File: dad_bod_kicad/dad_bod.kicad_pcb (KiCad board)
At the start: 2 copper layers, 89.2 x 89 mm, 132 parts, among them J1 Conn_01x01, J10 Conn_01x03_Male, J11 BNC5-J-P-GN-RA-BH2D, J12 USB4085-GF-A_REVA4, J13 Conn_01x03_Male, J14 Conn_01x03_Male, J2 Conn_01x01, J3 Conn_01x01, J4 Conn_01x01, J5 Conn_01x03_Male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

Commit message: fixing scheme & pcb disparities
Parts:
- C1: footprint ECQ-UBAF4747K_kicad:ECQ-UBAF474K-3_side -> kyuditsky_kicad:ECQ-UBAF474K-3_side
- D2, D3, D4, D5: footprint Diode_THT:D_DO-41_SOD81_P2.54mm_Vertical_AnodeUp -> Diode_THT:D_DO-41_SOD81_P2.54mm_Vertical_KathodeUp
- FB1, FB2, FB3: footprint Resistor_SMD:R_0603_1608Metric_Pad1.05x0.95mm_HandSolder -> Resistor_SMD:R_0805_2012Metric_Pad1.20x1.40mm_HandSolder
- J12: footprint kyuditsky_kicad_fp:GCT_USB4085-GF-A_REVA4 -> kyuditsky_kicad:GCT_USB4085-GF-A_REVA4
- U1: footprint kyuditsky_kicad_fp:SL1002A600SP -> kyuditsky_kicad:SL1002A600SP
- moved C3 13.1 mm to (130.3, 133.3)
- moved R1 13.1 mm to (122.7, 133.3)
- moved C18 13.1 mm to (122.0, 124.1)
- moved F1 13.1 mm to (145.4, 134.1)
- moved J3 13.1 mm to (94.5, 131.7)
- moved J4 13.1 mm to (109.2, 131.7)
- moved R13 13.1 mm to (126.7, 124.1)
- moved R40 13.1 mm to (137.7, 136.7)
- moved C17 13.1 mm to (141.5, 117.3)
- moved C34 13.1 mm to (138.4, 96.8)
- moved C42 13.1 mm to (141.0, 71.8)
- moved R10 13.1 mm to (133.6, 112.6)
- moved R12 13.1 mm to (133.6, 117.3)
- moved R28 13.1 mm to (133.6, 96.8)
- moved C10 13.1 mm to (122.2, 111.1)
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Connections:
- C18 pad 1: Net-(C18-Pad1) -> DIVin2-
- J12 pad A8: Net-(J12-PadA8) -> unconnected-(J12-PadA8)
- J12 pad B8: Net-(J12-PadB8) -> unconnected-(J12-PadB8)
- J13 pad 3: Net-(J13-Pad3) -> unconnected-(J13-Pad3)
- J14 pad 3: Net-(J14-Pad3) -> unconnected-(J14-Pad3)
- R13 pad 2: Net-(C18-Pad1) -> DIVin2-
- T1 pad 2: Net-(T1-Pad2) -> unconnected-(T1-Pad2)
- T1 pad 5: Net-(T1-Pad5) -> unconnected-(T1-Pad5)

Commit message: new layout
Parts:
- J9: footprint Connector_PinSocket_2.54mm:PinSocket_2x15_P2.54mm_Horizontal -> Connector_PinSocket_2.54mm:PinSocket_2x15_P2.54mm_Vertical
- moved RV1 80.3 mm to (78.5, 69.3), turned to 180 degrees
- moved U1 75.9 mm to (88.9, 68.6)
- moved T1 74.5 mm to (94.0, 79.0), turned to 90 degrees
- moved J11 71.5 mm to (97.8, 126.5), turned to 180 degrees
- moved D1 69.8 mm to (99.1, 68.3), turned to 0 degrees
- moved C2 69.6 mm to (98.3, 63.8), turned to 180 degrees
- moved C50 68.6 mm to (99.3, 115.8)
- moved C51 68.6 mm to (96.5, 115.8)
- moved C53 68.6 mm to (91.4, 115.8)
- moved Q3 68.6 mm to (102.4, 115.8)
- moved C52 68.6 mm to (94.0, 115.8)
- moved C49 68.6 mm to (88.9, 115.8)
- moved FB1 68.6 mm to (98.0, 119.0)
- moved FB3 68.6 mm to (98.1, 112.8)
- moved D6 65.8 mm to (73.9, 121.9), turned to -90 degrees
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
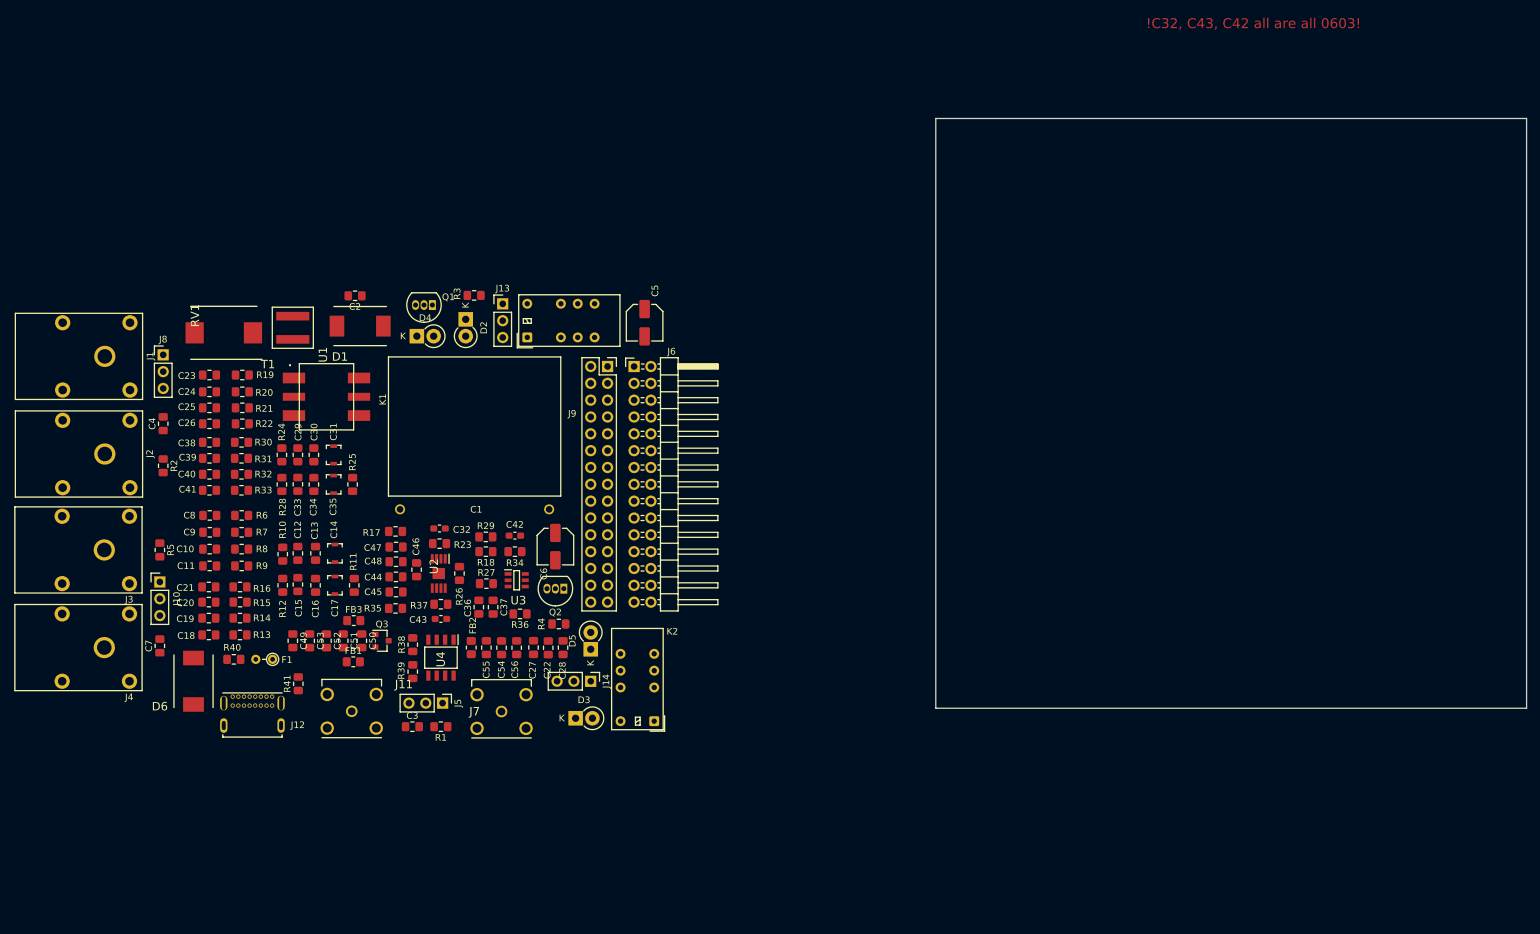
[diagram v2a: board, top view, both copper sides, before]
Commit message: Routed board
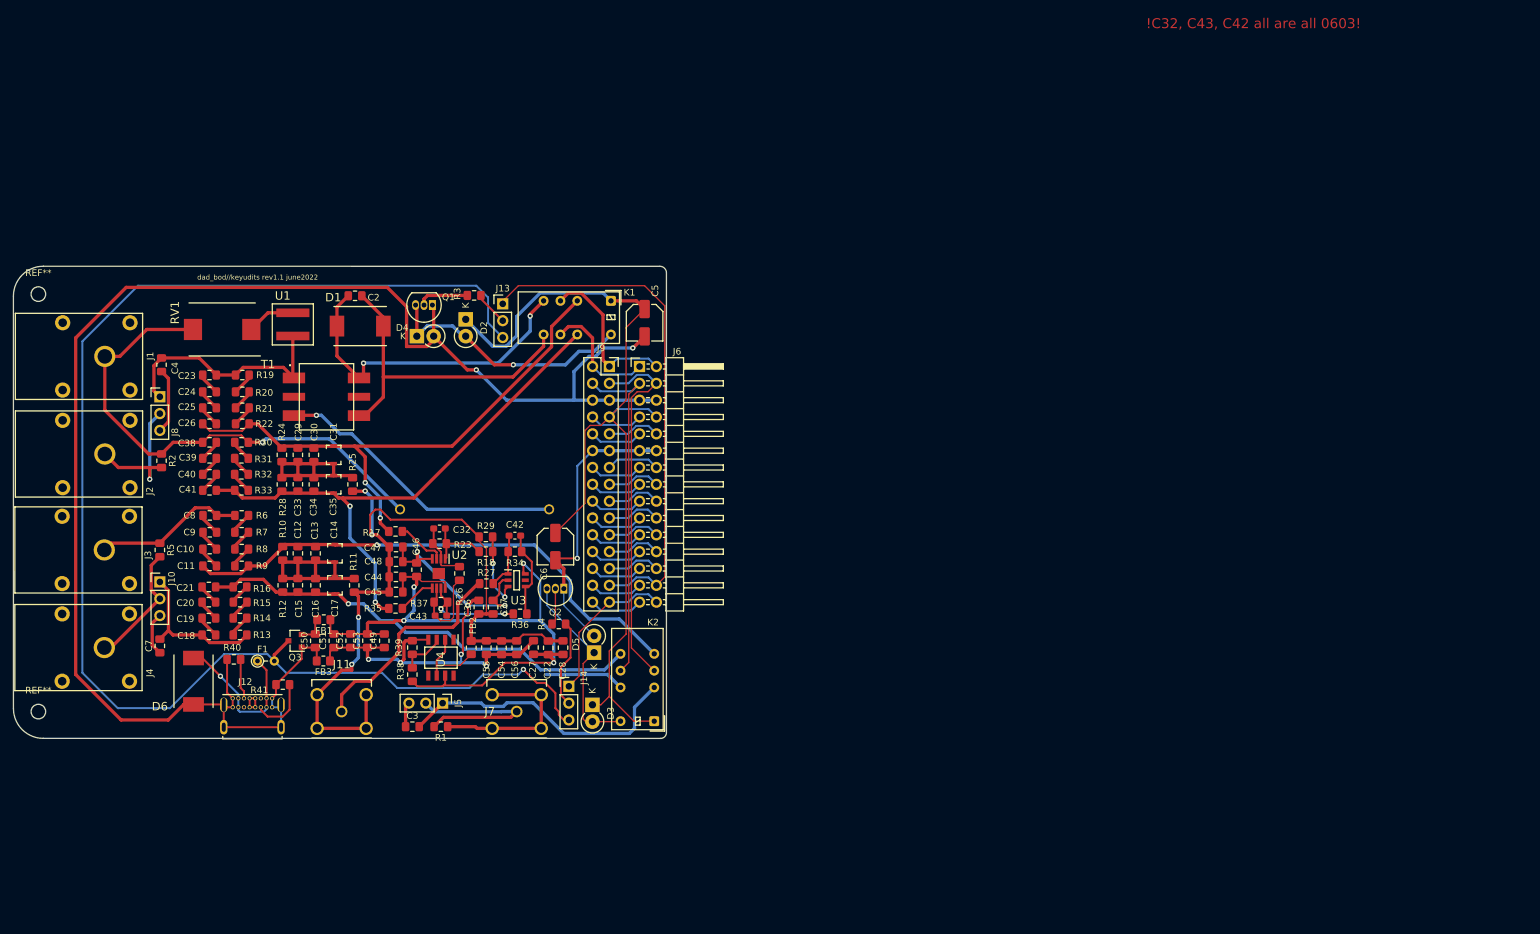
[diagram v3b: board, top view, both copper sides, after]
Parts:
- added REF**: MountingHole_2.2mm_M2, MountingHole:MountingHole_2.2mm_M2, F.Cu at (50.5, 63.5)
- added REF**: MountingHole_2.2mm_M2, MountingHole:MountingHole_2.2mm_M2, F.Cu at (50.5, 126.5)
- C1: moved to B.Cu
- moved C49 13.8 mm to (102.7, 115.8), turned to 90 degrees
- moved K1 13.8 mm to (136.9, 64.5), turned to -90 degrees
- moved Q3 13.1 mm to (89.2, 115.8), turned to 180 degrees
- moved C4 8.90 mm to (69.1, 74.2)
- moved C53 8.72 mm to (100.2, 115.8), turned to 90 degrees
- moved FB1 7.76 mm to (93.6, 112.6), turned to 180 degrees
- moved FB3 7.63 mm to (93.5, 118.9), turned to 180 degrees
- moved C50 7.03 mm to (92.3, 115.8), turned to 90 degrees
- moved J8 6.36 mm to (68.8, 79.0)
- moved R38 4.52 mm to (106.9, 120.9), turned to -90 degrees
- moved C52 3.64 mm to (97.6, 115.8), turned to 90 degrees
- moved R39 3.64 mm to (106.9, 116.8), turned to 90 degrees
- moved J14 3.39 mm to (130.6, 122.7), turned to 0 degrees
- moved D3 3.25 mm to (134.1, 125.5), turned to -90 degrees
- moved R41 2.34 mm to (87.4, 122.4), turned to 180 degrees
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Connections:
- J13 pad 2: V+ -> Net-(J13-Pad2)
- J13 pad 3: unconnected-(J13-Pad3) -> V+
- J14 pad 2: V+ -> Net-(R4-Pad1)
- J14 pad 3: unconnected-(J14-Pad3) -> V+
- J9 pad 1: scope1- -> scope1+
- J9 pad 10: waveform1 -> waveform2
- J9 pad 13: trigger2 -> trigger1
- J9 pad 14: trigger1 -> trigger2
- J9 pad 15: 8 -> 0
- J9 pad 16: 0 -> 8
- J9 pad 17: 9 -> 1
- J9 pad 18: 1 -> 9
- J9 pad 19: 10 -> 2
- J9 pad 2: scope1+ -> scope1-
- J9 pad 20: 2 -> 10
- J9 pad 21: 11 -> 3
- J9 pad 22: 3 -> 11
- J9 pad 23: 12 -> 4
- J9 pad 24: 4 -> 12
- J9 pad 25: 13 -> 5
- J9 pad 26: 5 -> 13
- J9 pad 27: 14 -> CV6
- J9 pad 28: CV6 -> 14
- J9 pad 29: 15 -> CV7
- J9 pad 3: scope2- -> scope2+
- J9 pad 30: CV7 -> 15
- J9 pad 4: scope2+ -> scope2-
- J9 pad 7: dad_V- -> relaypwr
- J9 pad 8: relaypwr -> dad_V-
- J9 pad 9: waveform2 -> waveform1
- R11 pad 1: GND -> GNDREF
- R3 pad 1: CV6 -> Net-(J13-Pad2)
- R4 pad 1: CV7 -> Net-(R4-Pad1)
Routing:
- net GND: track 0.00 -> 297.1 mm, vias 0 -> 3
- net V+: track 0.00 -> 213.4 mm, vias 0 -> 1
- net relaypwr: track 0.00 -> 138.8 mm
- net GNDREF: track 0.00 -> 116.2 mm, vias 0 -> 4
- net VCC: track 0.00 -> 104.6 mm, vias 0 -> 4
- net greg: track 0.00 -> 90.1 mm, vias 0 -> 7
- net DIVout1-: track 0.00 -> 86.2 mm, vias 0 -> 2
- net DIVout1+: track 0.00 -> 84.9 mm, vias 0 -> 2
- net DIVout2+: track 0.00 -> 79.0 mm, vias 0 -> 1
- net CV6: track 0.00 -> 77.9 mm
- net DIVin1-: track 0.00 -> 76.6 mm, vias 0 -> 1
- net DIVout2-: track 0.00 -> 68.2 mm, vias 0 -> 1
- net scope2+: track 0.00 -> 55.4 mm
- net scope2-: track 0.00 -> 52.6 mm
- net PLCout+: track 0.00 -> 49.6 mm, vias 0 -> 2
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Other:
- board size 89.2 x 89 mm -> 98.5 x 71.3 mm
- board text added: "JLCJLCJLCJLC"
- board text added: "dad_bod//keyudits rev1.1 june2022"

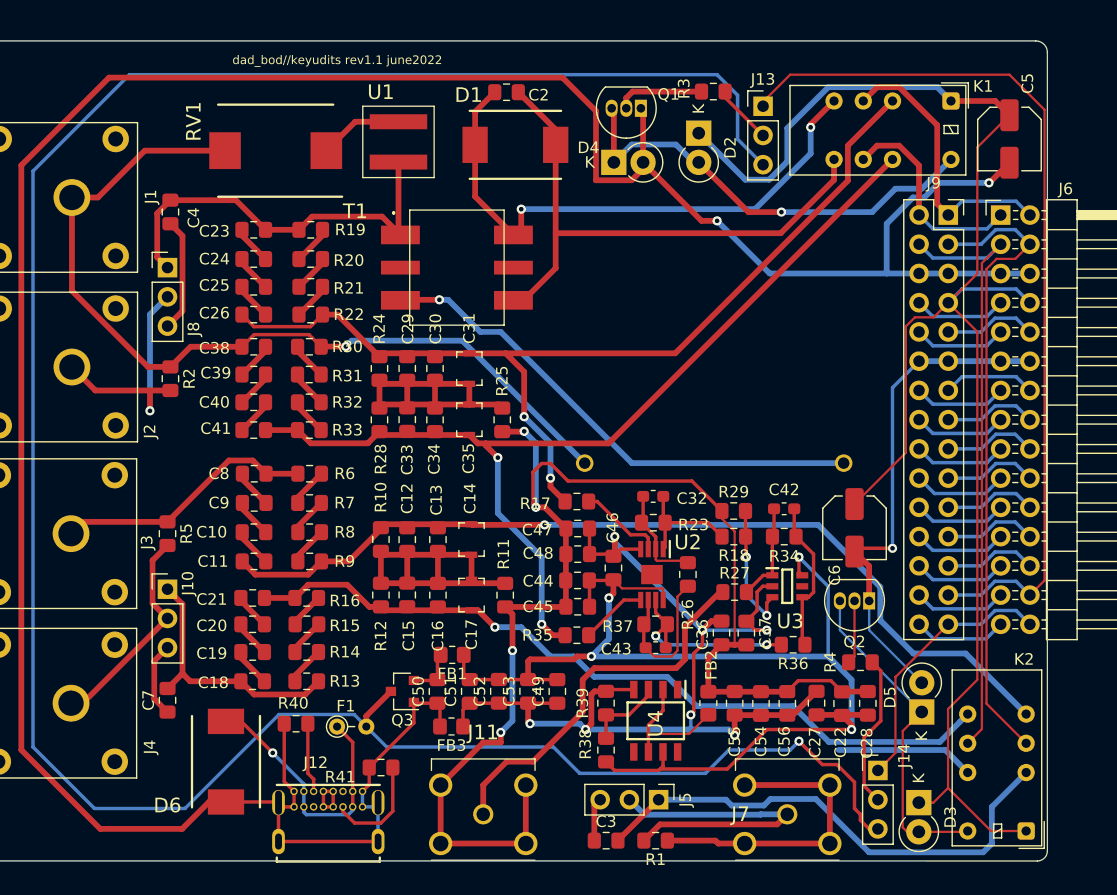
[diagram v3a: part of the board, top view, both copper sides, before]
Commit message: changed some routing/footprints after component selection
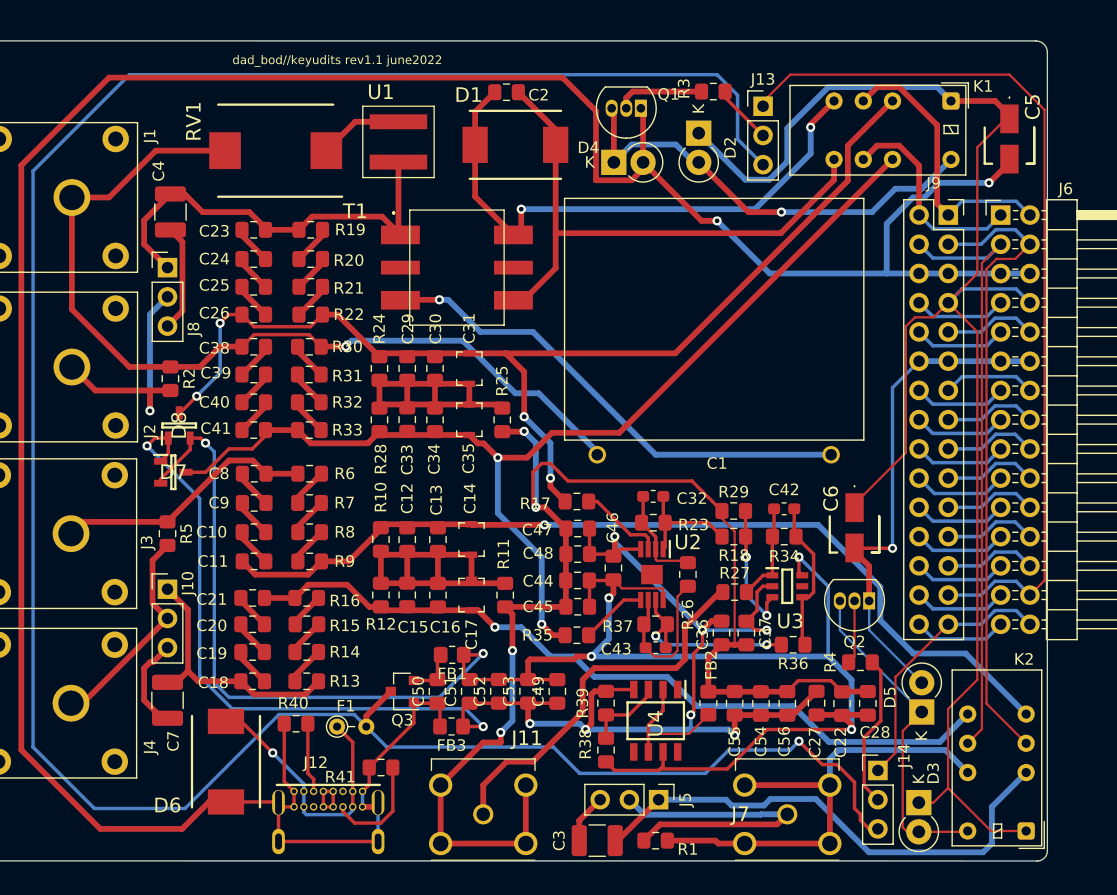
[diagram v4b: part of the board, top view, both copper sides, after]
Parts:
- added D7: BAV199-TP, kyuditsky_kicad:bav199_tp_SOT95P237X125-3N, F.Cu at (69.3, 96.8)
- added D8: BAV199-TP, kyuditsky_kicad:bav199_tp_SOT95P237X125-3N, F.Cu at (69.8, 92.7)
- C1: moved to F.Cu
- C3, C4, C7: footprint Capacitor_SMD:C_0805_2012Metric_Pad1.15x1.40mm_HandSolder -> Capacitor_SMD:C_1210_3225Metric_Pad1.33x2.70mm_HandSolder
- C5, C6: footprint Capacitor_SMD:C_Elec_5x5.4 -> kyuditsky_kicad:EEE1AA220WR
- D1: value SMCJ9.0CA -> SMCJ918.0CA
- moved C3 0.77 mm to (106.2, 128.8)
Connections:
- U3 pad 5: Net-(U3-Pad5) -> unconnected-(U3-Pad5)
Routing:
- net VCC: track 104.6 -> 159.4 mm, vias 4 -> 6
- net greg: track 90.1 -> 144.6 mm, vias 7 -> 9
- net DIVout1+: track 84.9 -> 96.4 mm, vias 2 -> 4
- net DIVout1-: track 86.2 -> 94.2 mm
- net BNCin-: track 38.7 -> 42.1 mm
- net DIVin1-: track 76.6 -> 78.5 mm
- net DIVin1+: track 35.3 -> 37.1 mm
- net Net-(C7-Pad1): track 6.55 -> 8.24 mm
- net Net-(C1-Pad2): track 44.4 -> 43.0 mm
- net Net-(C3-Pad1): track 3.77 -> 4.31 mm
- net Net-(C4-Pad1): track 9.86 -> 9.32 mm
